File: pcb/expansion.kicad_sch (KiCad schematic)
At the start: 25 parts, among them J10 PJ-063AH, J11 Conn_02x01, J12 Conn_02x01, J4 ESW-106-44-T-S, J5 PH2-06-UA, J6 ESW-112-44-T-S, J7 Conn_01x10, J8 ESW-112-44-T-S, J9 Conn_01x10, SW1 PTS810 SJM 250 SMTR LFS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

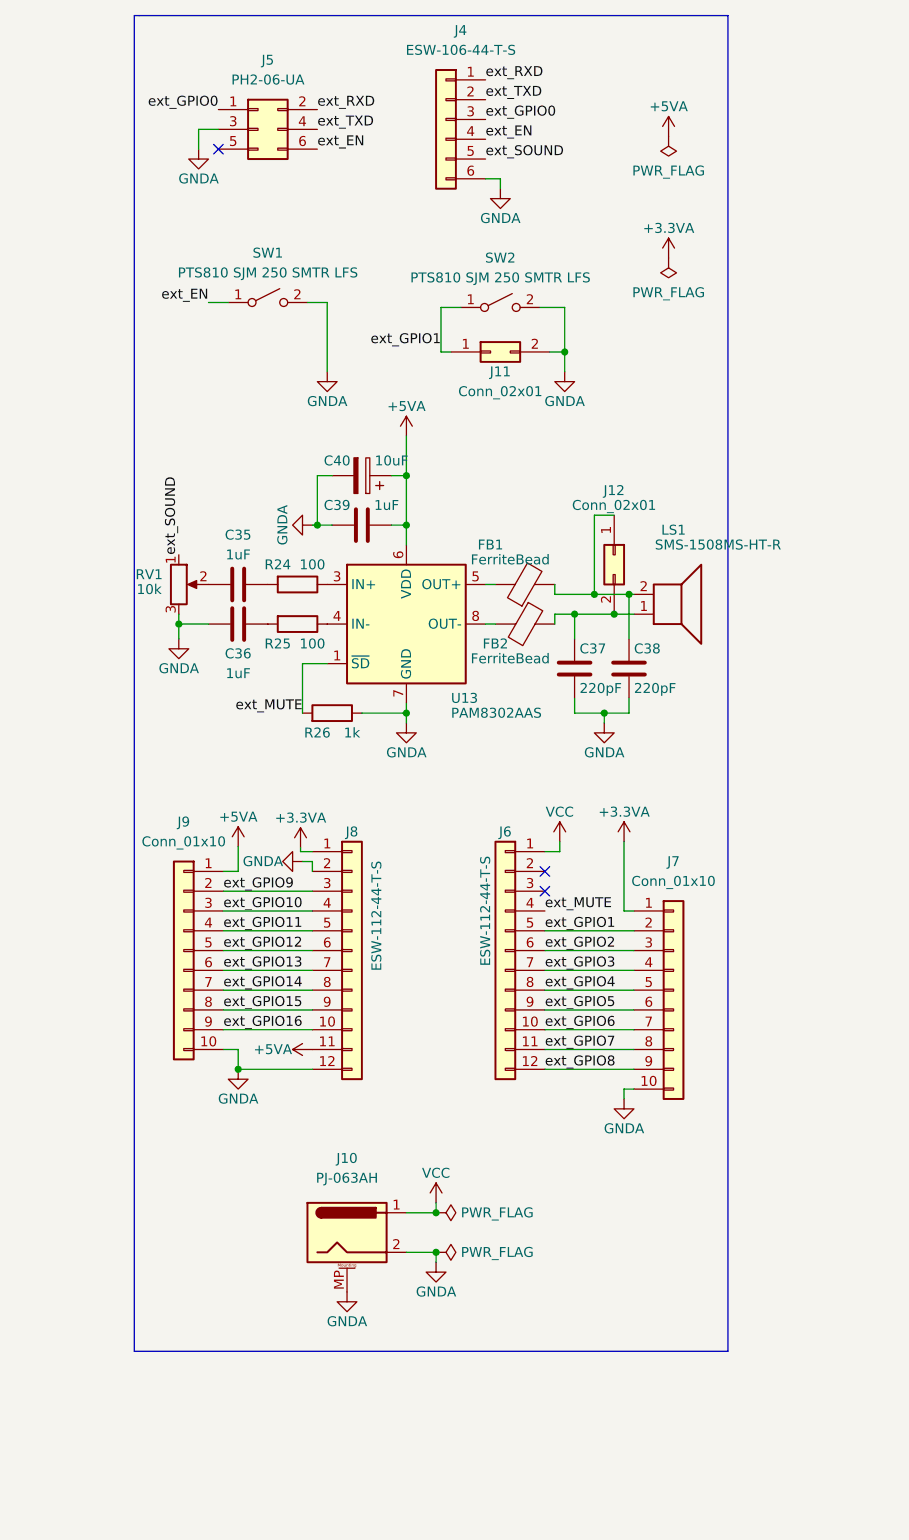
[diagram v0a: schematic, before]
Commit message: Bump the variable resistor to 20k, update the schematics, BOM for printing
Also marked C33 & D145 as NC (never could get it to work). It should
be replaced by a proper multi-lead RGB LED
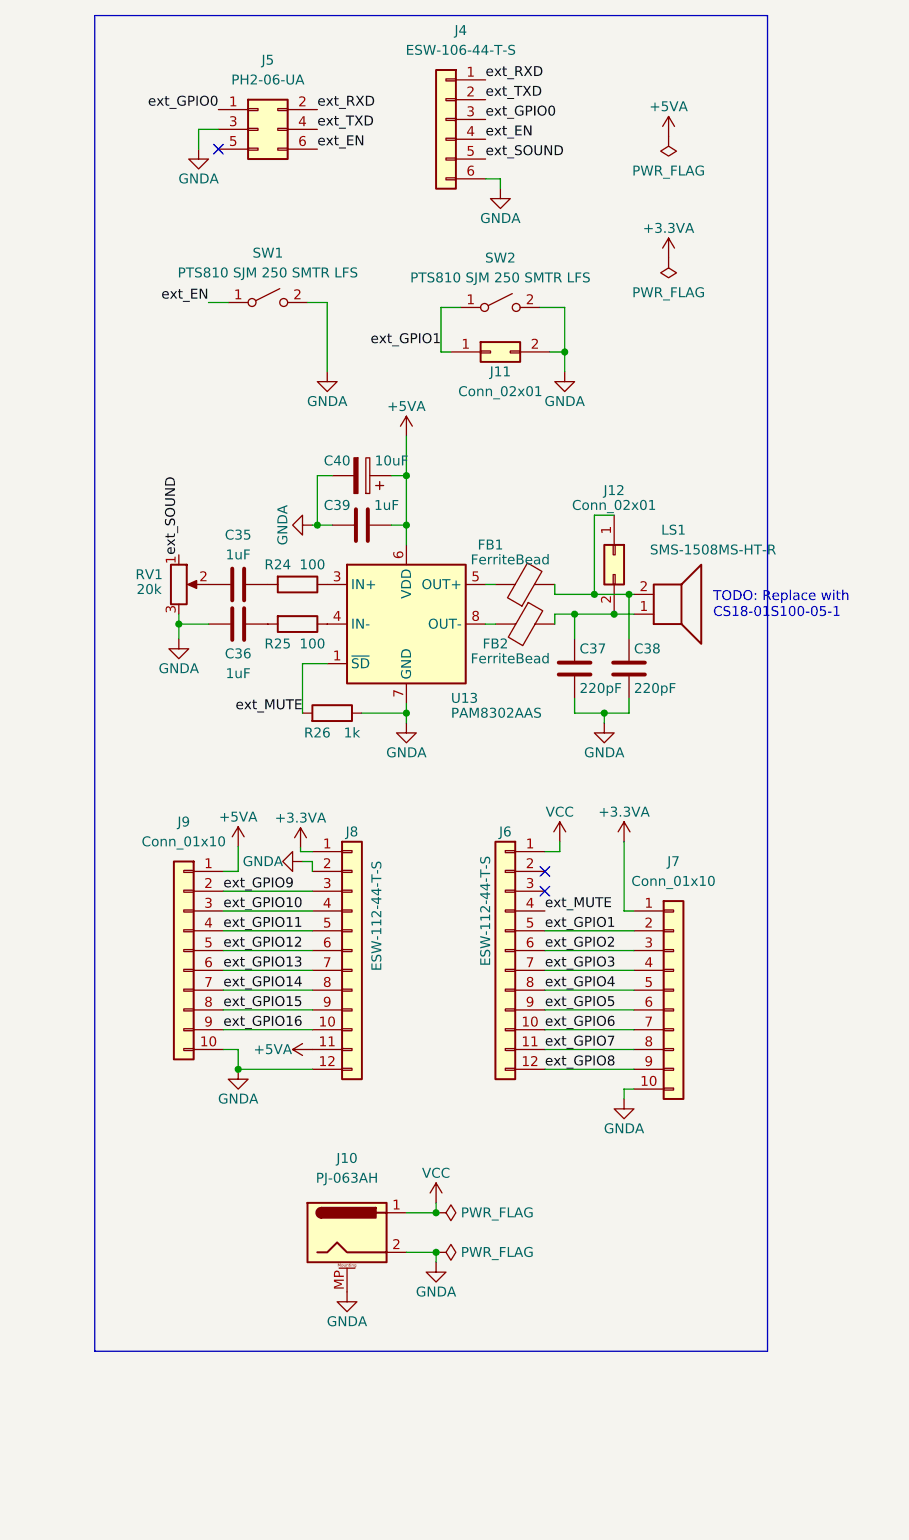
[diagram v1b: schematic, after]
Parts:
- RV1: value 10k -> 20k
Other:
- note added: "TODO: Replace with CS18-01S100-05-1"
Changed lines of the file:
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@@
     (stroke (width 0) (type default))
   )
-  (polyline (pts (xy 155.575 189.865) (xy 79.375 189.865))
+  (polyline (pts (xy 160.655 189.865) (xy 74.295 189.865))
     (stroke (width 0) (type default))
   )
@@
     (stroke (width 0) (type default))
   )
-  (polyline (pts (xy 79.375 18.415) (xy 80.01 18.415))
+  (polyline (pts (xy 74.295 18.415) (xy 74.295 18.415))
     (stroke (width 0) (type default))
   )
@@
     (stroke (width 0) (type default))
   )
-  (polyline (pts (xy 79.375 189.865) (xy 79.375 18.415))
+  (polyline (pts (xy 74.295 189.865) (xy 74.295 18.415))
     (stroke (width 0) (type default))
   )
@@
     (stroke (width 0) (type default))
   )
-  (polyline (pts (xy 80.01 18.415) (xy 155.575 18.415))
-    (stroke (width 0) (type default))
-  )
-  (polyline (pts (xy 155.575 18.415) (xy 155.575 189.865))
+  (polyline (pts (xy 74.295 18.415) (xy 160.655 18.415))
+    (stroke (width 0) (type default))
+  )
+  (polyline (pts (xy 160.655 18.415) (xy 160.655 189.865))
     (stroke (width 0) (type default))
   )
@@
   (wire (pts (xy 112.395 77.47) (xy 114.3 77.47))
     (stroke (width 0) (type default))
+  )
+  (text "TODO: Replace with\nCS18-01S100-05-1" (at 153.67 95.885 0)
+    (effects (font (size 1.27 1.27)) (justify left bottom))
   )
   (label "ext_GPIO1" (at 132.08 135.89 0) (fields_autoplaced)
@@
       (effects (font (size 1.27 1.27)))
     )
-    (property "Value" "10k" (at 81.28 92.075 0)
+    (property "Value" "20k" (at 81.28 92.075 0)
       (effects (font (size 1.27 1.27)))
     )
@@
       (effects (font (size 1.27 1.27)))
     )
-    (property "Value" "SMS-1508MS-HT-R" (at 154.305 86.36 0)
-      (effects (font (size 1.27 1.27)))
-    )
+    (property "Value" "SMS-1508MS-HT-R" (at 153.67 86.995 0)
+      (effects (font (size 1.27 1.27)))
+    )

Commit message: Normalized schematics for printing
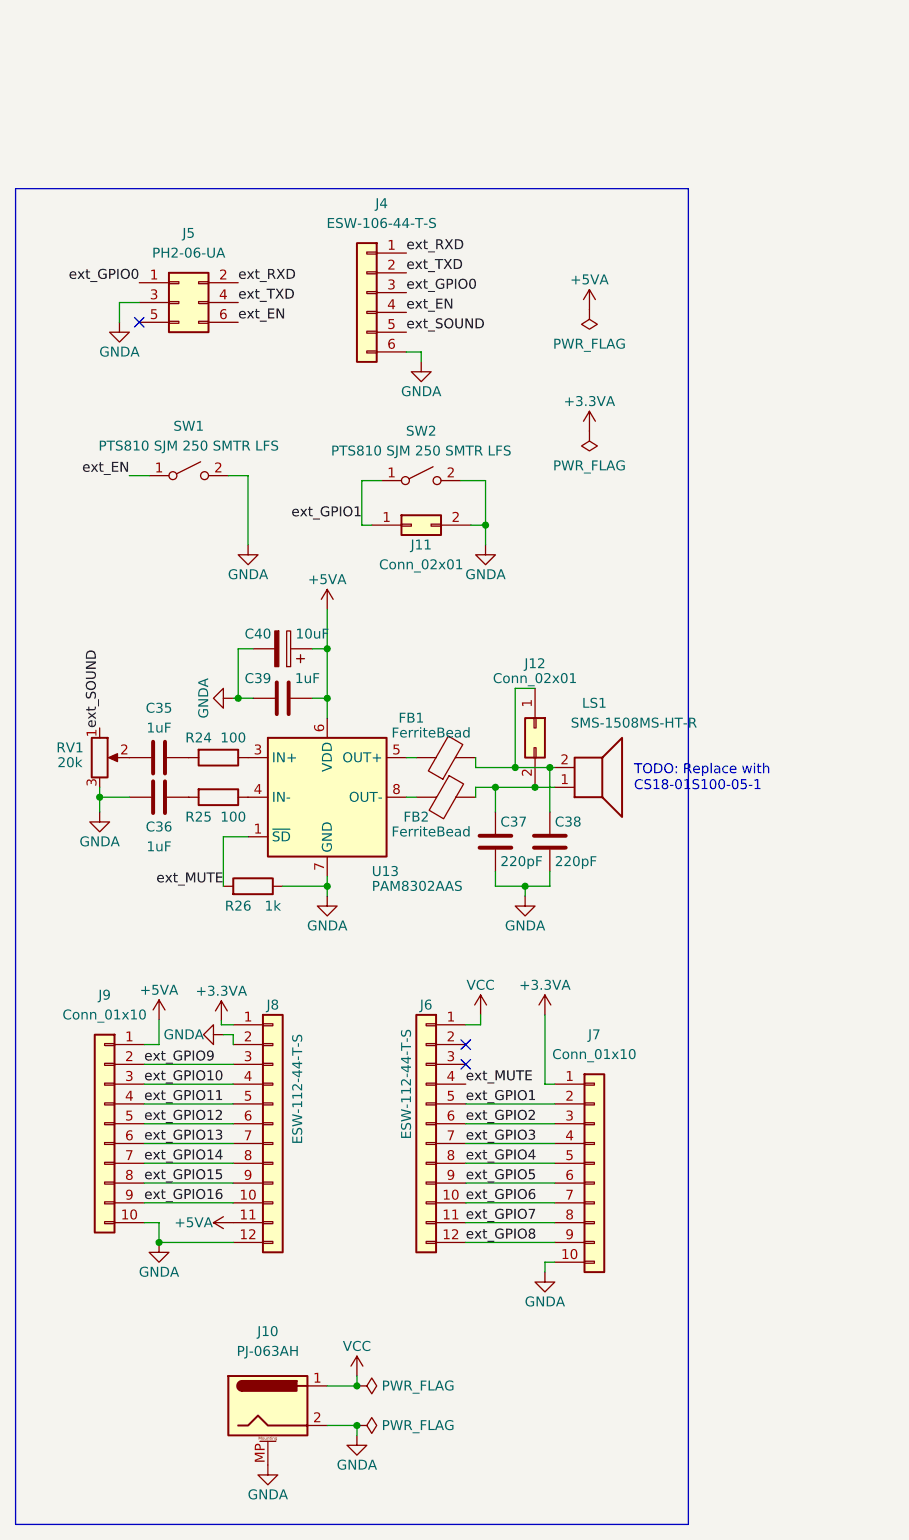
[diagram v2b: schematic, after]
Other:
- moved on the sheet: C35, C36, C37, C38, C39, C40, FB1, FB2, J10, J11, J12, J4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
